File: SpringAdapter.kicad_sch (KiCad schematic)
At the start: 18 parts, among them J1 USB_C_Receptacle_USB2.0, J2 Conn_02x04_Odd_Even, SW1 SW_DIP_x01, U1 AP2112K-3.3

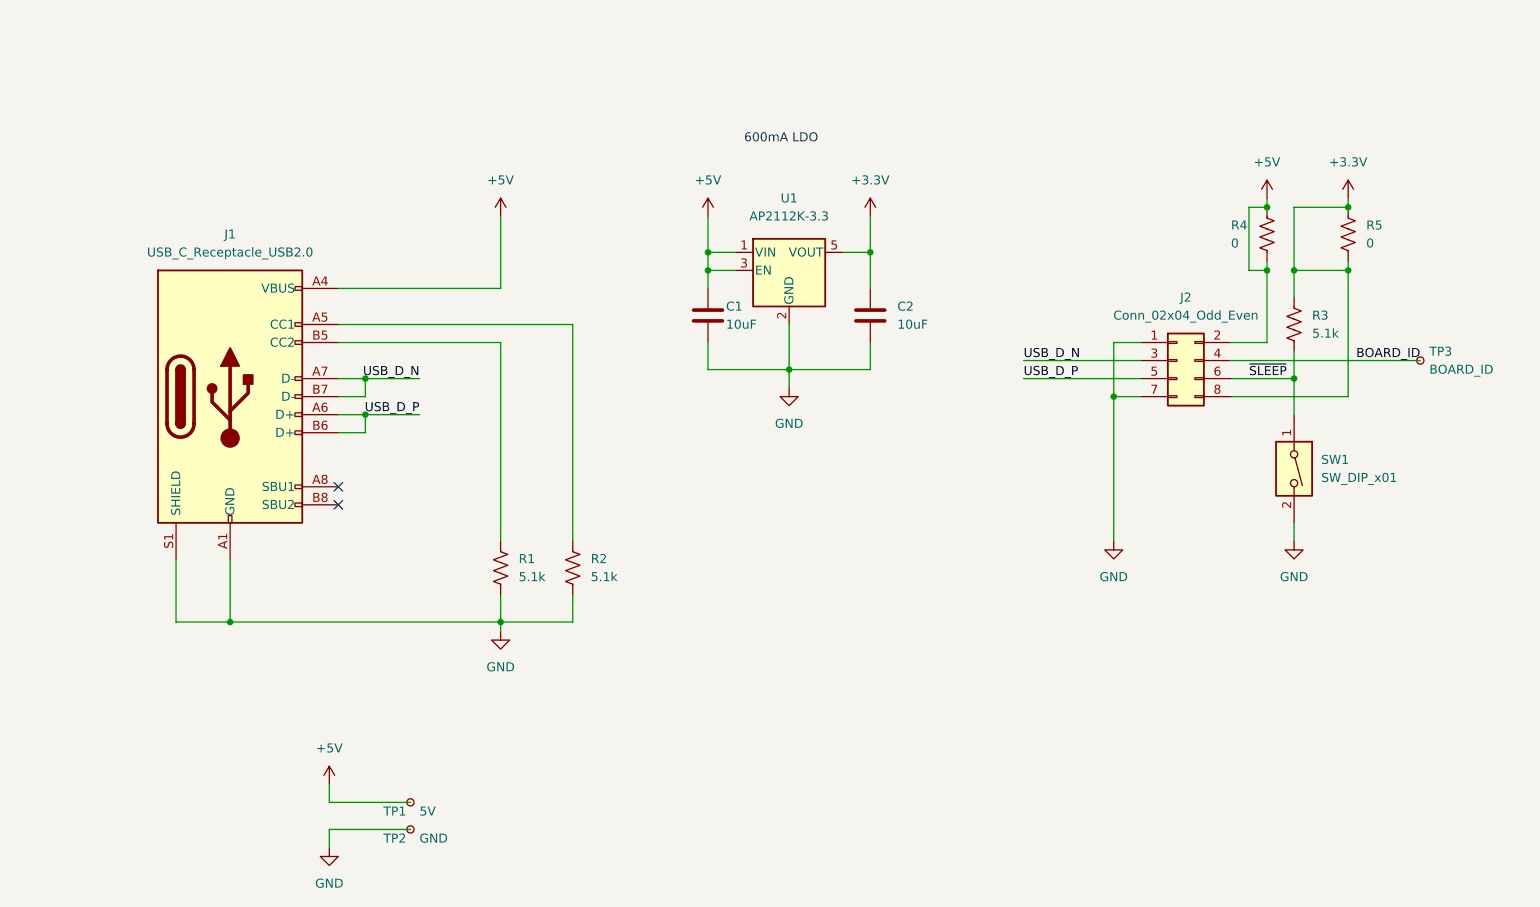
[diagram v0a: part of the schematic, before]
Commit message: Update repo to match JLCPCB parts, start adding USB hub
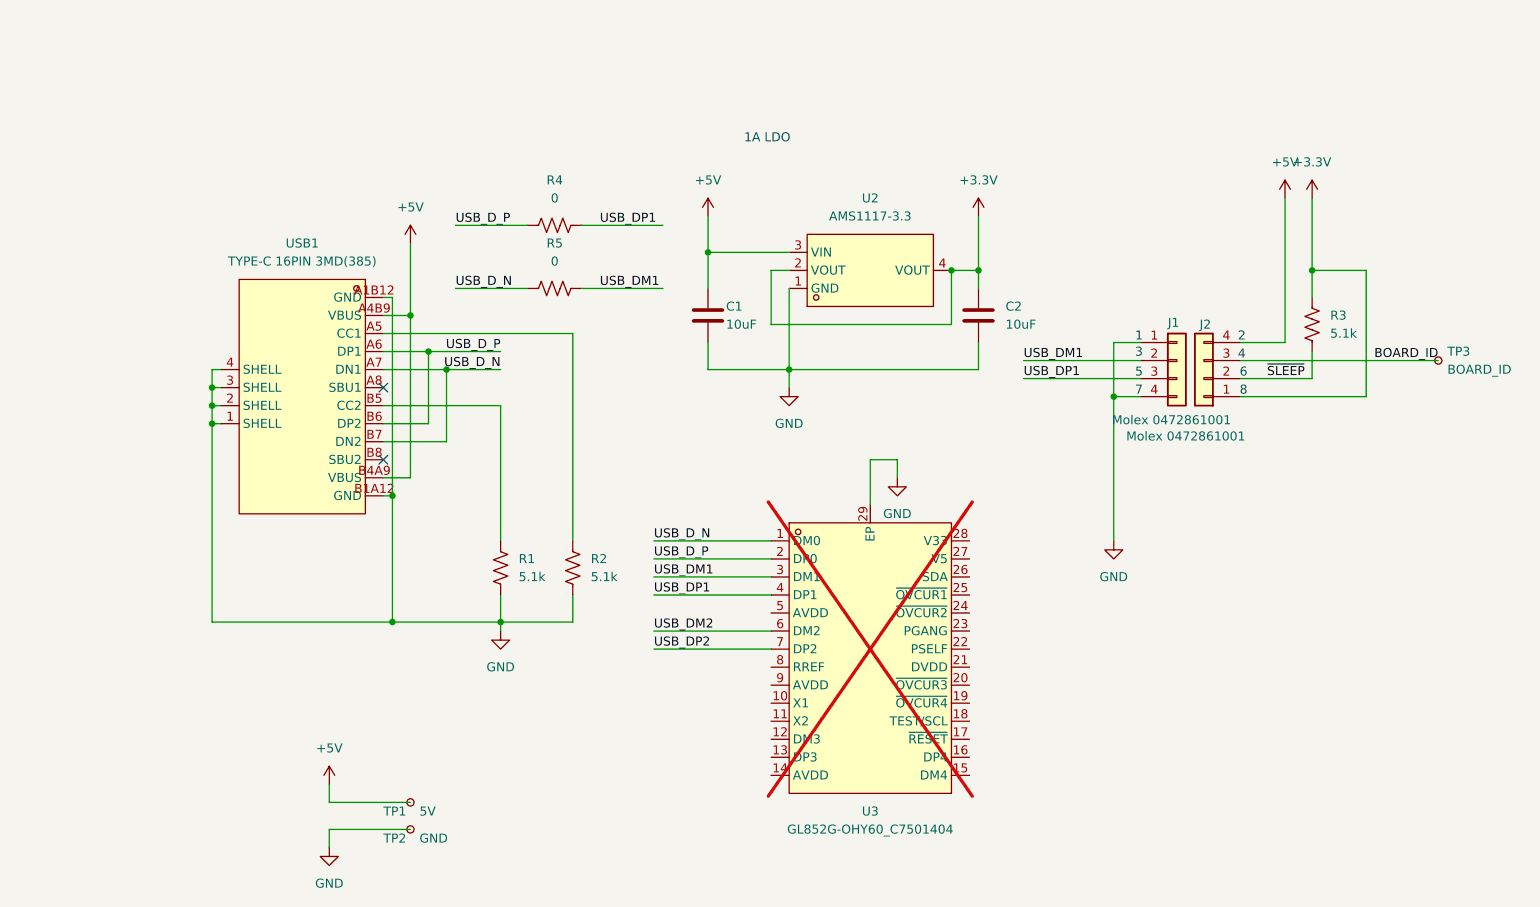
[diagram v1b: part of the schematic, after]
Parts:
- removed J1: USB_C_Receptacle_USB2.0, Connector_USB:USB_C_Receptacle_GCT_USB4085, symbol Connector:USB_C_Receptacle_USB2.0
- removed J2: Conn_02x04_Odd_Even, SpringAdapter:BP33242_2x4_P2.0mm, symbol Connector_Generic:Conn_02x04_Odd_Even
- removed SW1: SW_DIP_x01, Button_Switch_SMD:SW_DIP_SPSTx01_Slide_Omron_A6S-110x_W8.9mm_P2.54mm, symbol Switch:SW_DIP_x01
- removed U1: AP2112K-3.3, Package_TO_SOT_SMD:SOT-23-5, symbol Regulator_Linear:AP2112K-3.3
- added J1, J2: Molex 0472861001, ExternalMount:Molex_0472861001, symbol Connector_Generic:Conn_01x04
- added U2: AMS1117-3.3, ExternalMount:SOT-223-3_L6.5-W3.4-P2.30-LS7.0-BR, symbol ExternalMount:AMS1117-3.3
- added U3: GL852G-OHY60_C7501404, ExternalMount:QFN-28_L5.0-W5.0-P0.50-BL-EP, symbol ExternalMount:GL852G-OHY60_C7501404
- added USB1: TYPE-C 16PIN 3MD(385), ExternalMount:USB-C-SMD_TYPE-C16PIN, symbol ExternalMount:TYPE-C16PIN3MD(385)
- R4, R5: footprint Resistor_SMD:R_1206_3216Metric -> Resistor_SMD:R_0603_1608Metric
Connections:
- net +3.3V: now also J2.1 (Pin_1), U2.2 (VOUT), U2.4 (VOUT); no longer R5.1, R5.2
- net +5V: now also J2.4 (Pin_4), U2.3 (VIN), USB1.A4B9 (VBUS), USB1.B4A9 (VBUS); no longer R4.1, R4.2
- net BOARD_ID: now also J2.3 (Pin_3)
- net GND: now also J1.1 (Pin_1), J1.4 (Pin_4), U2.1 (GND), U3.29 (EP), USB1.1 (SHELL), USB1.2 (SHELL), USB1.3 (SHELL), USB1.4 (SHELL), USB1.A1B12 (GND), USB1.B1A12 (GND)
- net USB_D_N: now also R5.1, U3.1 (DM0), USB1.A7 (DN1), USB1.B7 (DN2)
- net USB_D_P: now also R4.1, U3.2 (DP0), USB1.A6 (DP1), USB1.B6 (DP2)
- net ~{SLEEP}: now also J2.2 (Pin_2)
- net at R1.1: now also USB1.B5 (CC2)
- net at R2.1: now also USB1.A5 (CC1)
- new net USB_DM1: J1.2 (Pin_2), R5.2, U3.3 (DM1)
- new net USB_DM2: U3.6 (DM2)
- new net USB_DP1: J1.3 (Pin_3), R4.2, U3.4 (DP1)
- new net USB_DP2: U3.7 (DP2)
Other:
- note added: "1"
- note added: "1A LDO"
- note added: "2"
- note added: "3"
- note added: "4"
- note added: "5"
- note added: "6"
- note added: "7"
- note added: "8"
- note removed: "600mA LDO"
- moved on the sheet: C2, R3, TP3

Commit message: First version complete
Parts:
- removed TP1: 5V, TestPoint:TestPoint_Pad_D1.0mm, symbol Connector:TestPoint_Small
- removed TP2: GND, TestPoint:TestPoint_Pad_D1.0mm, symbol Connector:TestPoint_Small
- removed TP3: BOARD_ID, TestPoint:TestPoint_Pad_D1.0mm, symbol Connector:TestPoint_Small
- removed U2: AMS1117-3.3, ExternalMount:SOT-223-3_L6.5-W3.4-P2.30-LS7.0-BR, symbol ExternalMount:AMS1117-3.3
- added C10, C11: 22pF, Capacitor_SMD:C_0402_1005Metric, symbol Device:C
- added C12, C14, C16, C18, C20, C3, C4, C5, C7, C9: 100nF, Capacitor_SMD:C_0402_1005Metric, symbol Device:C
- added C13, C15, C17, C19, C6, C8: 10uF, Capacitor_SMD:C_0603_1608Metric, symbol Device:C
- added H5, H6: MountingHole, MountingHole:MountingHole_5mm, symbol Mechanical:MountingHole
- added H7, H8: MountingHole, MountingHole:MountingHole_2.5mm, symbol Mechanical:MountingHole
- added J3, J4: Molex 0472861001, ExternalMount:Molex_0472861001, symbol Connector_Generic:Conn_01x04
- added L1: 10u, Inductor_SMD:L_0805_2012Metric, symbol Device:L_Small
- added R10: 20k, Resistor_SMD:R_0402_1005Metric, symbol Device:R_US
- added R11: 100k, Resistor_SMD:R_0402_1005Metric, symbol Device:R_US
- added R12: 0, Resistor_SMD:R_0402_1005Metric, symbol Device:R_US
- added R13, R8, R9: 10k, Resistor_SMD:R_0402_1005Metric, symbol Device:R_US
- added R6: 680 1%, Resistor_SMD:R_0603_1608Metric, symbol Device:R_US
- added R7: 47k, Resistor_SMD:R_0402_1005Metric, symbol Device:R_US
- added U1: XC6206P332MR-G, Package_TO_SOT_SMD:SOT-23-3, symbol Regulator_Linear:XC6206PxxxMR
- added X1: 12MHz, ExternalMount:OSC-SMD_4P-L3.2-W2.5-BL, symbol ExternalMount:X322512MSB4SI
- C1, C2: LCSC Part (none) -> C96446
- J1, J2: LCSC Part (none) -> C6961828
- R1, R2: footprint Resistor_SMD:R_0603_1608Metric -> Resistor_SMD:R_0402_1005Metric; LCSC Part (none) -> C25905
- R3: footprint Resistor_SMD:R_0603_1608Metric -> Resistor_SMD:R_0402_1005Metric; LCSC Part (none) -> C25905; now not fitted
- R4, R5: footprint Resistor_SMD:R_0603_1608Metric -> Resistor_SMD:R_0402_1005Metric; LCSC Part (none) -> C17168; now not fitted
- U3: now fitted
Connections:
- net +3.3V: now also U3.21 (DVDD), U3.28 (V33), C6.1, C7.1, L1.2, R11.1, R13.1; no longer C2.1, J2.1 (Pin_1)
- net +5V: now also U3.27 (V5), C13.1, C14.1, C17.1, C18.1, C8.1, C9.1, J4.4 (Pin_4), R8.1, R9.1, U1.3 (VI)
- net GND: now also U3.18 (TEST/SCL), C10.2, C11.2, C12.2, C13.2, C14.2, C15.2, C16.2, C17.2, C18.2, C19.2, C20.2, C3.2, C4.2, C5.2, C6.2, C7.2, C8.2, C9.2, J3.1 (Pin_1), J3.4 (Pin_4), R10.2, R6.2, R7.2, U1.1 (GND), X1.2 (GND), X1.4 (GND)
- net USB_DM2: now also J3.2 (Pin_2)
- net USB_DP2: now also J3.3 (Pin_3)
- net ~{SLEEP}: now also J4.2 (Pin_2), R12.2
- net at U3.10 (X1): now also C11.1, X1.3 (OSC2)
- net at U3.11 (X2): now also C10.1, X1.1 (OSC1)
- net AVDD: now reaches U3.14 (AVDD)
- net AVDD: now also U3.5 (AVDD), U3.9 (AVDD), C3.1, C4.1, C5.1, L1.1
- net RESET: now reaches U3.17 (~{RESET})
- net RESET: now also C12.1, R7.1, R8.2
- net at U3.22 (PSELF): now also R13.2
- net at U3.23 (PGANG): now also R11.2, R12.1
- net OVCURR: now reaches U3.25 (~{OVCUR1})
- net OVCURR: now also R10.1, R9.2
- net RREF: now reaches U3.8 (RREF)
- net RREF: now also R6.1
- net BOARD_ID: no longer names the net of J2.3 (Pin_3)
- new net +3.3VP: C15.1, C16.1, C19.1, C2.1, C20.1, J2.1 (Pin_1), J4.1 (Pin_1), U1.2 (VO)
- no-connect marks 2 -> 12
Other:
- note added: "200mA LDO"
- note added: "BOARD ID"
- note added: "Each Input Module can draw 500mA on 5V rail and 100mA on 3.3V rail. We ask for 1.5A on 5V via USB-C and can supply 1A on 3.3V."
- note added: "Input Module Connector 1"
- note added: "Input Module Connector 2"
- note added: "Place cap near each AVDD pin"
- note added: "USB 2.0 HUB"
- note added: "USB-C INPUT"
- note removed: "1A LDO"
- moved on the sheet: C1, C2, H1, H2, H3, H4, J1, J2, R1, R2, USB1

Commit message: DFM work
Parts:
- added H10, H11, H12, H9: Tooling Hole, ExternalMount:JLCPCB Tooling Hole, symbol Mechanical:MountingHole
- H1, H2, H3, H4, H5, H6, H7, H8: now left out of the parts list
- U3: JLCPCB Rotation Offset (none) -> -90

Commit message: Documentation updates!
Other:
- note added: "Each Input Module can draw 500mA on 5V rail and 100mA on 3.3V rail. We ask for 1.5A on 5V via USB-C and can supply 200mA on 3.3V."
- note added: "For a lower-cost version that only supports the lefthand Input Module Connector (#1), all the components in this block and the Input Module Connector 2 block can be omitted, and R3/R4/R5 should be populated."
- note removed: "Each Input Module can draw 500mA on 5V rail and 100mA on 3.3V rail. We ask for 1.5A on 5V via USB-C and can supply 1A on 3.3V."
- moved on the sheet: R3
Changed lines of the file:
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@@
 	)
 	(junction
+		(at 124.46 158.75)
+		(diameter 0)
+		(color 0 0 0 0)
+	)
+	(junction
 		(at 36.83 186.69)
 		(diameter 0)
@@
 	(wire
 		(pts
-			(xy 113.03 30.48) (xy 113.03 34.29)
+			(xy 124.46 154.94) (xy 124.46 158.75)
 		)
 		(stroke
@@
 	(wire
 		(pts
-			(xy 92.71 34.29) (xy 113.03 34.29)
-		)
-		(stroke
-			(width 0)
-			(type default)
-		)
-	)
-	(wire
-		(pts
 			(xy 200.66 130.81) (xy 200.66 139.7)
 		)
@@
 	(wire
 		(pts
-			(xy 113.03 20.32) (xy 113.03 22.86)
+			(xy 124.46 144.78) (xy 124.46 147.32)
 		)
 		(stroke
@@
 		)
 	)
-	(text "Each Input Module can draw 500mA on 5V rail and 100mA on 3.3V rail.\nWe ask for 1.5A on 5V via USB-C and can supply 1A on 3.3V."
+	(text "Each Input Module can draw 500mA on 5V rail and 100mA on 3.3V rail.\nWe ask for 1.5A on 5V via USB-C and can supply 200mA on 3.3V."
 		(exclude_from_sim no)
 		(at 212.09 86.106 0)
@@
 		)
 	)
+	(text "For a lower-cost version that only supports the lefthand Input Module\nConnector (#1), all the components in this block and the Input Module\nConnector 2 block can be omitted, and R3/R4/R5 should be populated."
+		(exclude_from_sim no)
+		(at 76.708 123.19 0)
+		(effects
+			(font
+				(size 1.27 1.27)
+			)
+		)
+	)
 	(text "1"
 		(exclude_from_sim no)
@@
 		)
 	)
-	(label "~{SLEEP}"
-		(at 93.98 34.29 0)
-		(fields_autoplaced yes)
-		(effects
-			(font
-				(size 1.27 1.27)
-			)
-			(justify left bottom)
-		)
-	)
 	(label "USB_DP1"
 		(at 43.18 153.67 0)
@@
 	(symbol
 		(lib_id "power:+3.3V")
-		(at 113.03 20.32 0)
+		(at 124.46 144.78 0)
 		(unit 1)
 		(exclude_from_sim no)
@@
 		(fields_autoplaced yes)
 		(property "Reference" "#PWR03"
-			(at 113.03 24.13 0)
+			(at 124.46 148.59 0)
 			(effects
 				(font
@@
 		)
 		(property "Value" "+3.3V"
-			(at 113.03 15.24 0)
+			(at 124.46 139.7 0)
 			(effects
 				(font
@@
 		)
 		(property "Footprint" ""
-			(at 113.03 20.32 0)
+			(at 124.46 144.78 0)
 			(effects
 				(font
@@
 		)
 		(property "Datasheet" ""
-			(at 113.03 20.32 0)
+			(at 124.46 144.78 0)
 			(effects
 				(font
@@
 		)
 		(property "Description" "Power symbol creates a global label with name \"+3.3V\""
-			(at 113.03 20.32 0)
+			(at 124.46 144.78 0)
 			(effects
 				(font
@@
 	(symbol
 		(lib_id "Device:R_US")
-		(at 113.03 26.67 0)
+		(at 124.46 151.13 0)
 		(unit 1)
 		(exclude_from_sim no)
@@
 		(dnp yes)
 		(property "Reference" "R3"
-			(at 115.57 25.4 0)
+			(at 127 149.86 0)
 			(effects
 				(font
@@
 		)
 		(property "Value" "5.1k"
-			(at 115.57 27.94 0)
+			(at 127 152.4 0)
 			(effects
 				(font
@@
 		)
 		(property "Footprint" "Resistor_SMD:R_0402_1005Metric"
-			(at 114.046 26.924 90)
+			(at 125.476 151.384 90)
 			(effects
 				(font
@@
 		)
 		(property "Datasheet" "~"
-			(at 113.03 26.67 0)
+			(at 124.46 151.13 0)
 			(effects
 				(font
@@
 		)
 		(property "Description" "Resistor, US symbol"
-			(at 113.03 26.67 0)
+			(at 124.46 151.13 0)
 			(effects
 				(font
@@
 		)
 		(property "LCSC Part" "C25905"
-			(at 113.03 26.67 0)
+			(at 124.46 151.13 0)
 			(effects
 				(font

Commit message: Schematic/board v2: add CH32V003 to read board ID and control power/sleep
The microcontroller allows us to actually monitor the BOARD_ID and USB CC1/2
lines to monitor and control power consumption.  It uses the unused 3rd
USB port on the hub.  ESD protection has also been added to all touchable
connectors.  A programming connector for the CH32V003 has been added based
on the same molex 2mm-pitch spring connector we use for input modules.

CH32V003 USB interface based on
  https://github.com/cnlohr/rv003usb
and we expect to flash the USB bootloader on this to allow it to be
reprogrammed by the end user:
  https://github.com/cnlohr/rv003usb/tree/master/bootloader

FreeCAD model updated.  Switched to realthunder FreeCAD fork since
it handled the parametric dependency updates better.
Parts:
- removed H5, H6: MountingHole, MountingHole:MountingHole_5mm, symbol Mechanical:MountingHole
- removed H7, H8: MountingHole, MountingHole:MountingHole_2.5mm, symbol Mechanical:MountingHole
- removed R12: 0, Resistor_SMD:R_0402_1005Metric, symbol Device:R_US
- added C1, C24, C25, C4: 10uF, Capacitor_SMD:C_0603_1608Metric, symbol Device:C
- added C23: 100nF, Capacitor_SMD:C_0402_1005Metric, symbol Device:C
- added D1, D2, D3, D4, D5, D6: USBLC6-2P6_C2827693, ExternalMount:SOT-666-6_L1.6-W1.2-P0.50-LS1.6-BL, symbol ExternalMount:USBLC6-2P6_C2827693
- added H10, H9: MountingHole, ExternalMount:MountingHole_5mm_no_keepout, symbol Mechanical:MountingHole
- added H11, H12: MountingHole, MountingHole:MountingHole_2.5mm, symbol Mechanical:MountingHole
- added LED1: Input Module Power, ExternalMount:LED0603-RD-YELLOW, symbol ExternalMount:19-213_Y2C-CQ2R2L_3T(CY)
- added R16: 1.5k 5%, Resistor_SMD:R_0402_1005Metric, symbol Device:R_US
- added R17: 330, Resistor_SMD:R_0402_1005Metric, symbol Device:R_US
- added R18: 5.1k, Resistor_SMD:R_0402_1005Metric, symbol Device:R_US
- added R19, R20, R21: 100k, Resistor_SMD:R_0402_1005Metric, symbol Device:R_US
- added R2, R3: 4.7k, Resistor_SMD:R_0402_1005Metric, symbol Device:R_US
- added R8: 0, Resistor_SMD:R_0402_1005Metric, symbol Device:R_US
- added TP1: 5V, TestPoint:TestPoint_Pad_1.5x1.5mm, symbol Connector:TestPoint
- added TP2: n/c, TestPoint:TestPoint_Pad_1.5x1.5mm, symbol Connector:TestPoint
- added TP3: SWIO, TestPoint:TestPoint_Pad_1.5x1.5mm, symbol Connector:TestPoint
- added TP4: GND, TestPoint:TestPoint_Pad_1.5x1.5mm, symbol Connector:TestPoint
- added U2, U5: SY6280AAC, ExternalMount:SOT-23-5_L3.0-W1.7-P0.95-LS2.8-BL, symbol ExternalMount:SY6280AAC
- added U4: CH32V003F4U6, ExternalMount:QFN-20_L3.0-W3.0-P0.40-TL-EP1.7, symbol ExternalMount:CH32V003F4U6
- H1, H2: footprint MountingHole:MountingHole_5mm -> ExternalMount:MountingHole_5mm_no_keepout
- R1: renamed from R3; value 5.1k -> 10k; LCSC Part C25905 -> C25744; now fitted
- renumbered C9 to C10, C3 to C11, C4 to C12, C5 to C13, C6 to C14, C7 to C15, C12 to C16, C19 to C18, C18 to C19, C1 to C2, C11 to C21, C10 to C22, C2 to C3, C13 to C5, C15 to C6, C14 to C7, C16 to C8, C8 to C9, H9 to H5, H10 to H6, H11 to H7, H12 to H8, R8 to R10, R10 to R11, R7 to R12, R6 to R13, R13 to R14, R11 to R15, R1 to R5, R2 to R6, R5 to R7
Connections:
- net +3.3V: now also C23.1, U4.6 (VDD); no longer R1.1
- net +3.3VP: now also R1.1, D3.5 (VBUS), D6.5 (VBUS), R17.1, R19.1, R20.1
- net +5V: now also C1.1, C25.1, R8.1, TP1.1, U2.1 (OUT), U5.5 (IN); no longer C17.1, C19.1, C2.1, C5.1, C7.1, J2.4 (Pin_4), J4.4 (Pin_4), U1.3 (VI), USB1.A4B9 (VBUS), USB1.B4A9 (VBUS)
- net GND: now also C1.2, C23.2, C24.2, C25.2, C4.2, D1.2 (GND), D2.2 (GND), D3.2 (GND), D4.2 (GND), D5.2 (GND), D6.2 (GND), LED1.1 (C), R18.1, R21.2, R3.2, TP4.1, U2.2 (GND), U4.21 (VSS), U4.4 (VSS), U5.2 (GND)
- net USB_DM1: now also D2.4 (I/O2); no longer J1.2 (Pin_2)
- net USB_DM2: now also D5.4 (I/O2); no longer J3.2 (Pin_2)
- net USB_DP1: now also D2.6 (I/O1); no longer J1.3 (Pin_3)
- net USB_DP2: now also D5.6 (I/O1); no longer J3.3 (Pin_3)
- net USB_D_N: now also D4.4 (I/O2); no longer USB1.A7 (DN1), USB1.B7 (DN2)
- net USB_D_P: now also D1.6 (I/O1); no longer USB1.A6 (DP1), USB1.B6 (DP2)
- net ~{SLEEP}: now also D3.4 (I/O2), D6.4 (I/O2), U4.13 (PC6/MOSI/T1CH1CH3N_); no longer J2.2 (Pin_2), J4.2 (Pin_2), R1.2
- net BOARD_ID1_UNP: now reaches J2.3 (Pin_3)
- net BOARD_ID1_UNP: now also D3.1 (I/O1), R20.2
- net USB_DM3: now reaches U3.12 (DM3)
- net USB_DM3: now also R16.2, U4.18 (PD4/A7/UCK/T2CH1ETR)
- net USB_DP3: now reaches U3.13 (DP3)
- net USB_DP3: now also U4.17 (PD3/A4/T2CH2/AETR)
- net PGANG: now reaches R15.2, U3.23 (PGANG)
- net PGANG: now also U4.12 (PC5/SCK/T1ETR/T2CH1ETR_)
- net CC1_UNP: now reaches USB1.A5 (CC1)
- net CC1_UNP: now also R5.1, D4.1 (I/O1); no longer R6.1
- net CC2_UNP: now reaches USB1.B5 (CC2)
- net CC2_UNP: now also R6.1, D1.3 (I/O2); no longer R5.1
- net BOARD_ID2_UNP: now reaches J4.3 (Pin_3)
- net BOARD_ID2_UNP: now also D6.1 (I/O1), R19.2
- new net: D5.1 (I/O1), J3.3 (Pin_3)
- new net: D5.3 (I/O2), J3.2 (Pin_2)
- new net: LED1.2 (A), R17.2
- new net: D2.3 (I/O2), J1.2 (Pin_2)
- new net: D2.1 (I/O1), J1.3 (Pin_3)
- new net: R2.2, U2.4 (EN)
- new net: R3.1, U2.3 (ISET)
- new net: R18.2, U5.3 (ISET)
- new net +5VP: C17.1, C19.1, C2.1, C24.1, C5.1, C7.1, D2.5 (VBUS), D5.5 (VBUS), J2.4 (Pin_4), J4.4 (Pin_4), R8.2, U1.3 (VI), U5.1 (OUT)
- new net BOARD_ID1: D3.6 (I/O1), U4.11 (PC4/A2/T1CH4/MCO)
- new net BOARD_ID2: D6.6 (I/O1), U4.16 (PD2/A3/T1CH1/T2CH3_)
- new net CC1: D4.6 (I/O1), U4.3 (PA2/OSCO/A0/T1CH2N)
- new net CC2: D1.4 (I/O2), U4.2 (PA1/OSCI/A1)
- new net DPU: R16.1, U4.19 (PD5/A5/UTX)
- new net PWREN: R21.1, U4.20 (PD6/A6/URX), U5.4 (EN)
- new net SWIO: TP3.1, U4.15 (PD1/SWIO/AETR2)
- new net USB_DN_UNP: D4.3 (I/O2), USB1.A7 (DN1), USB1.B7 (DN2)
- new net USB_DP_UNP: D1.1 (I/O1), USB1.A6 (DP1), USB1.B6 (DP2)
- new net V-UNFUSED: C4.1, D1.5 (VBUS), D4.5 (VBUS), R2.1, U2.5 (IN), USB1.A4B9 (VBUS), USB1.B4A9 (VBUS)
- new net ~{SLEEP1_UNP}: D3.3 (I/O2), J2.2 (Pin_2), R1.2
- new net ~{SLEEP2_UNP}: D6.3 (I/O2), J4.2 (Pin_2)
- no-connect marks 12 -> 16
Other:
- note added: "Board ID voltage divider"
- note added: "CC pull-down resistors don't need ESD protection"
- note added: "Current limiter: 1.45A"
- note added: "For a lower-cost version that only supports the lefthand Input Module Connector (#1), all the components below the dashed line can be omitted, and R4/R7/R8 should be populated."
- note added: "Load switching/Current limiter: 1.33A"
- note added: "SLEEP pull-up doesn't need ESD protection"
- note added: "These resistors don't need to be protected from ESD, and the routing is easier if they are on the "unprotected" side"
- note removed: "BOARD ID"
- note removed: "For a lower-cost version that only supports the lefthand Input Module Connector (#1), all the components in this block and the Input Module Connector 2 block can be omitted, and R3/R4/R5 should be populated."
- moved on the sheet: C17, C18, C19, C2, C20, C3, C5, C6, C7, C8, H1, H2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

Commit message: Fix part rotations for assembly
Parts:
- U2, U5: JLCPCB Rotation Offset (none) -> 180
- U4: JLCPCB Rotation Offset (none) -> -90
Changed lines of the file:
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@@
 			)
 		)
+		(property "JLCPCB Rotation Offset" "-90"
+			(at 175.26 193.04 0)
+			(effects
+				(font
+					(size 1.27 1.27)
+				)
+				(hide yes)
+			)
+		)
 		(pin "10"
 		)
@@
 			)
 		)
+		(property "JLCPCB Rotation Offset" "180"
+			(at 88.9 54.61 0)
+			(effects
+				(font
+					(size 1.27 1.27)
+				)
+				(hide yes)
+			)
+		)
 		(pin "2"
 		)
@@
 			(at 379.73 209.55 0)
 			(effects
+				(font
+					(size 1.27 1.27)
+				)
+				(hide yes)
+			)
+		)
+		(property "JLCPCB Rotation Offset" "180"
+			(at 379.73 209.55 0)
+			(effects
